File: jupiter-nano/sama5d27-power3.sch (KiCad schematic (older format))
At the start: 25 parts, among them U4 MIC5247-2.0YM5-TR

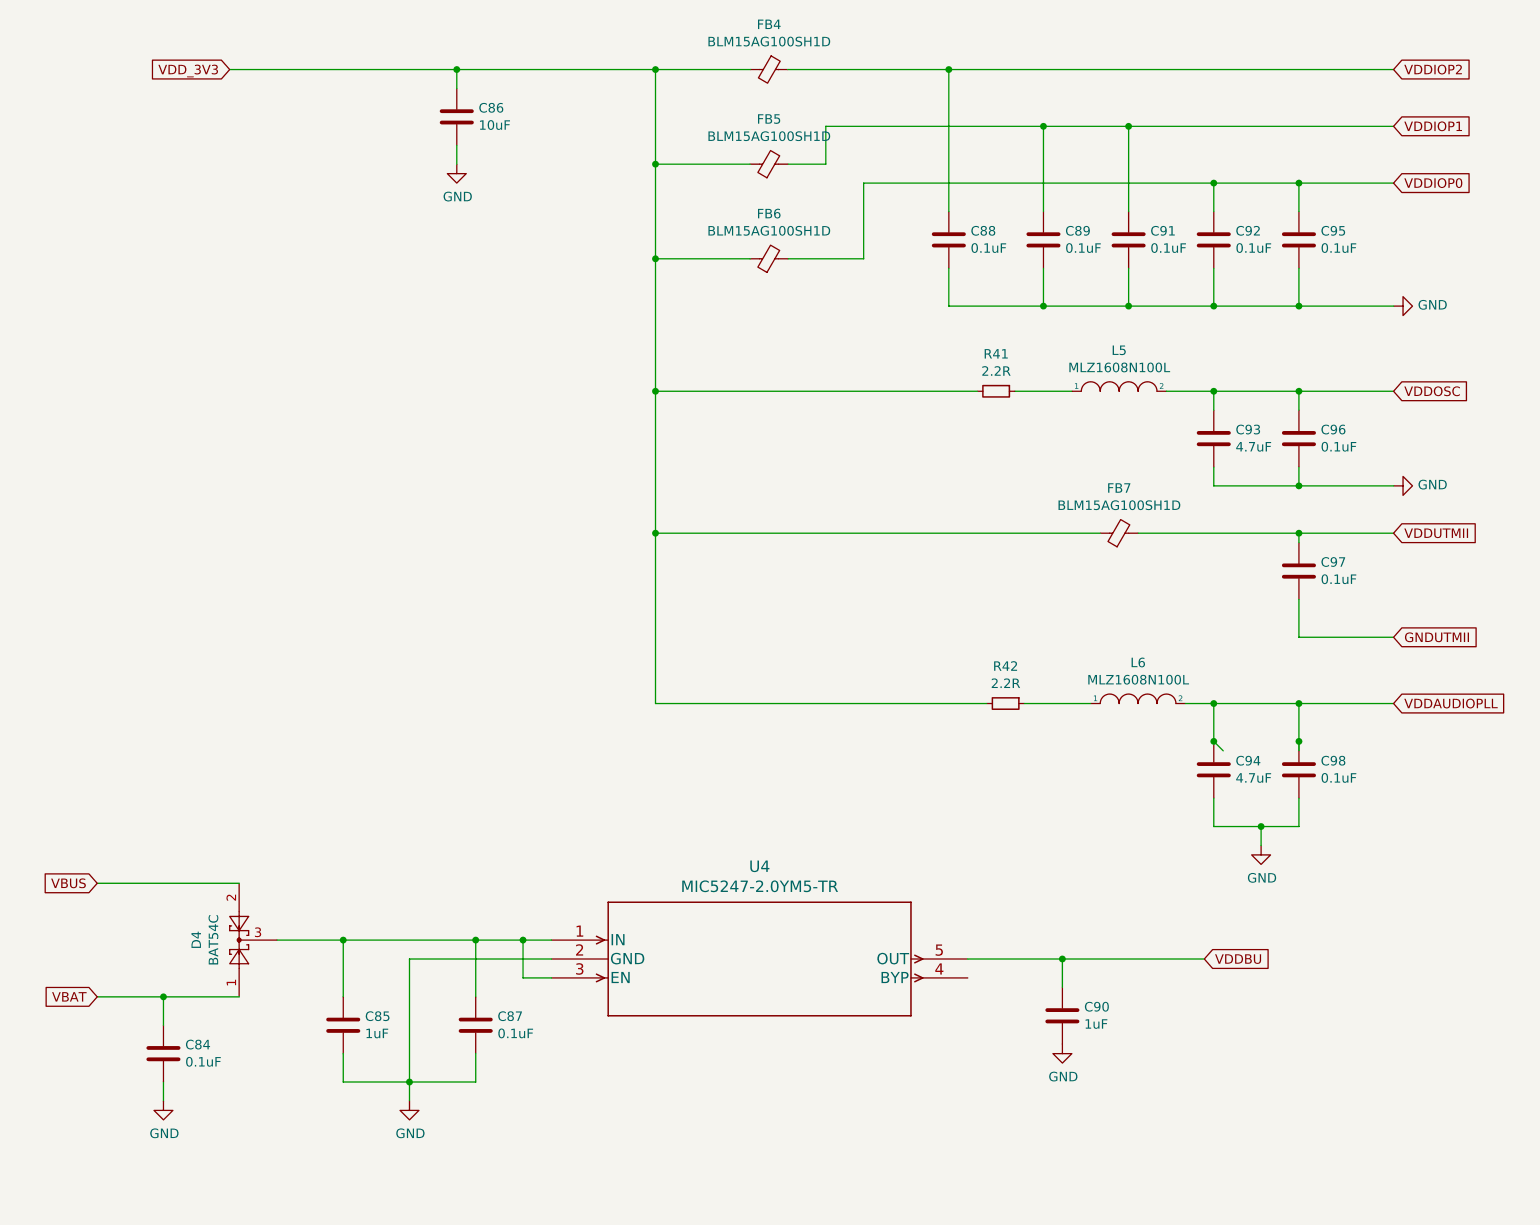
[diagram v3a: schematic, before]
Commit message: added at24csw080 I2C EEPROM UUID chip
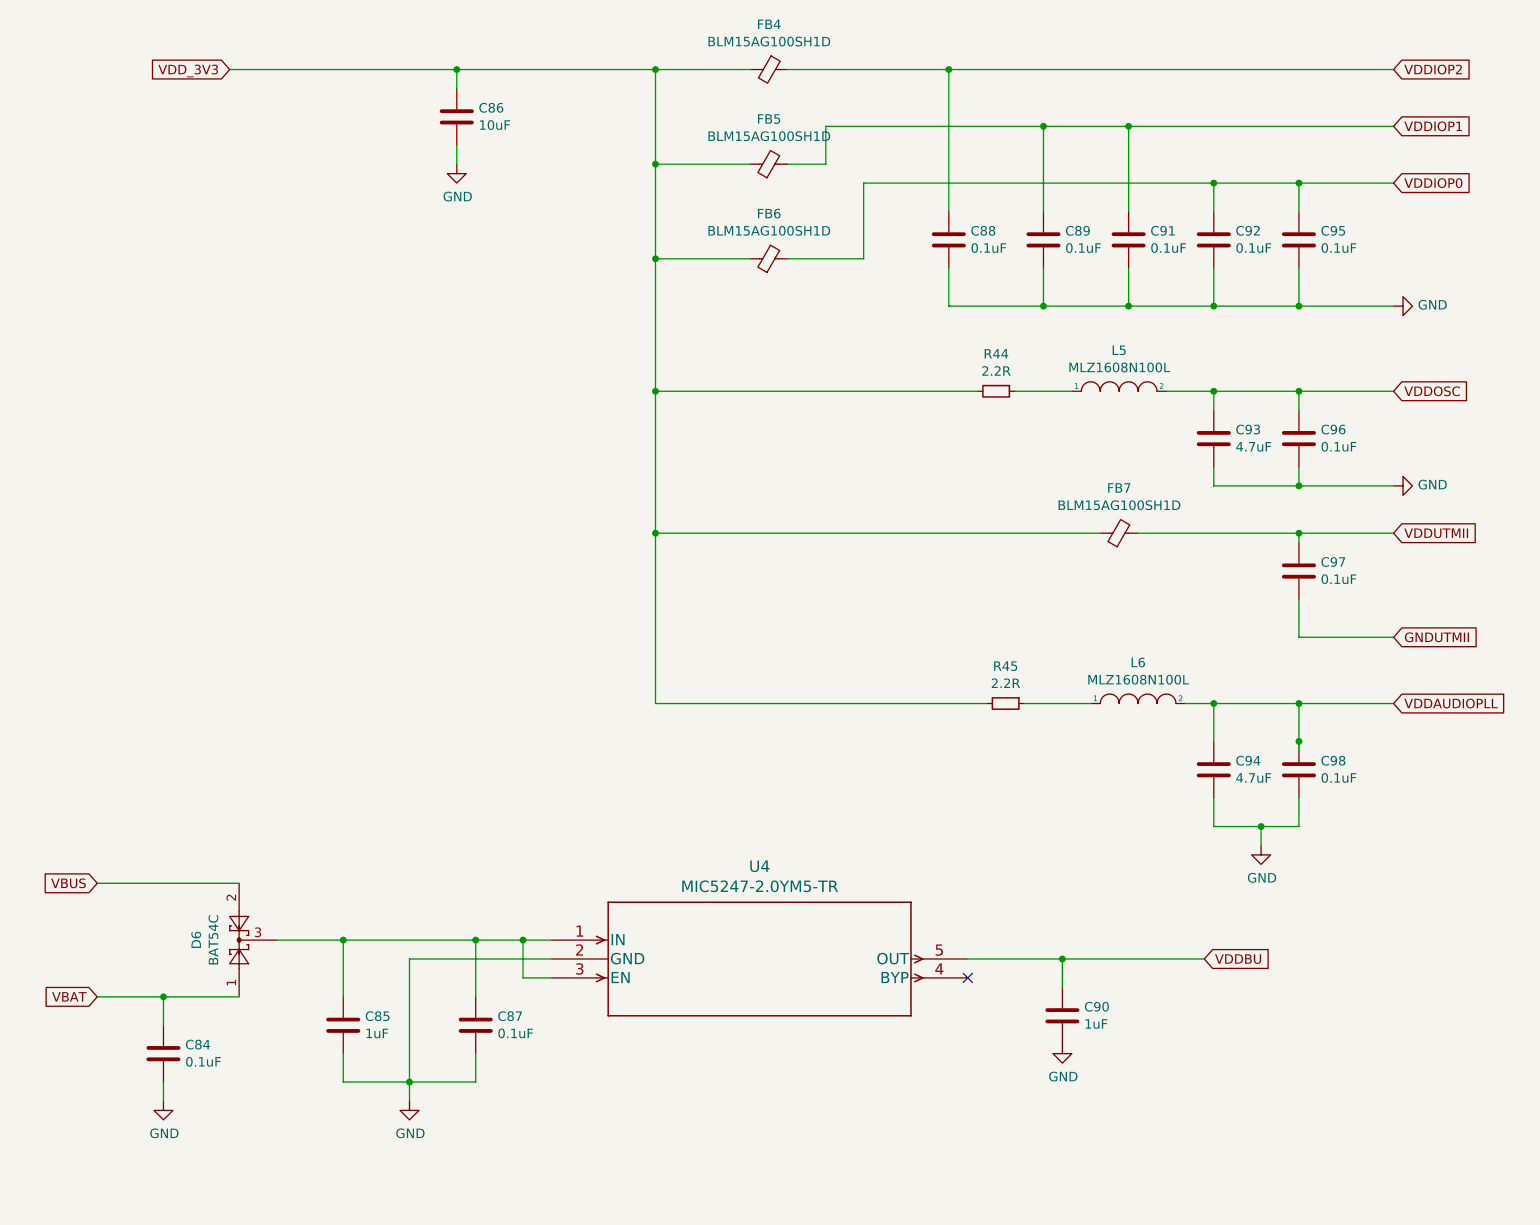
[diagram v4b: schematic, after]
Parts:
- renumbered D4 to D6, R41 to R44, R42 to R45
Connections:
- no-connect marks 0 -> 1
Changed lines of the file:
@@
 P 2200 5600
 AR Path="/5F395E67/5FD7EF78" Ref="D?"  Part="1"
-AR Path="/5FD740BF/5FD7EF78" Ref="D4"  Part="1"
-F 0 "D4" H 2200 5825 50  0000 C CNN
+AR Path="/5FD740BF/5FD7EF78" Ref="D6"  Part="1"
+F 0 "D6" H 2200 5825 50  0000 C CNN
 F 1 "BAT54C" H 2200 5734 50  0000 C CNN
 F 2 "Package_TO_SOT_SMD:SOT-23" H 2275 5725 50  0001 L CNN
@@
 	6550 5700 7300 5700
 $Comp
-L power:GND #PWR072
+L power:GND #PWR073
 U 1 1 5FD98CB8
 P 6550 6150
-F 0 "#PWR072" H 6550 5900 50  0001 C CNN
+F 0 "#PWR073" H 6550 5900 50  0001 C CNN
 F 1 "GND" H 6555 5977 50  0000 C CNN
 F 2 "" H 6550 6150 50  0001 C CNN
@@
 	3100 6350 3100 6450
 $Comp
-L power:GND #PWR070
+L power:GND #PWR071
 U 1 1 5FD9D491
 P 3100 6450
-F 0 "#PWR070" H 3100 6200 50  0001 C CNN
+F 0 "#PWR071" H 3100 6200 50  0001 C CNN
 F 1 "GND" H 3105 6277 50  0000 C CNN
 F 2 "" H 3100 6450 50  0001 C CNN
@@
 	1800 5900 1450 5900
 $Comp
-L power:GND #PWR069
+L power:GND #PWR070
 U 1 1 5FDA258D
 P 1800 6450
-F 0 "#PWR069" H 1800 6200 50  0001 C CNN
+F 0 "#PWR070" H 1800 6200 50  0001 C CNN
 F 1 "GND" H 1805 6277 50  0000 C CNN
 F 2 "" H 1800 6450 50  0001 C CNN
@@
 	5950 2250 6450 2250
 $Comp
-L power:GND #PWR074
+L power:GND #PWR075
 U 1 1 5FDA8E26
 P 8300 2250
-F 0 "#PWR074" H 8300 2000 50  0001 C CNN
+F 0 "#PWR075" H 8300 2000 50  0001 C CNN
 F 1 "GND" V 8305 2122 50  0000 R CNN
 F 2 "" H 8300 2250 50  0001 C CNN
@@
 Wire Wire Line
 	7800 4550 7800 4350
-Connection ~ 7350 4550
-Wire Wire Line
-	7350 4550 7400 4600
 Wire Wire Line
 	7600 5000 7600 5100
@@
 	7600 5000 7800 5000
 $Comp
-L power:GND #PWR073
+L power:GND #PWR074
 U 1 1 5FE0FC03
 P 7600 5100
-F 0 "#PWR073" H 7600 4850 50  0001 C CNN
+F 0 "#PWR074" H 7600 4850 50  0001 C CNN
 F 1 "GND" H 7605 4927 50  0000 C CNN
 F 2 "" H 7600 5100 50  0001 C CNN
@@
 	7800 3200 8300 3200
 $Comp
-L power:GND #PWR075
+L power:GND #PWR076
 U 1 1 5FE13F3A
 P 8300 3200
-F 0 "#PWR075" H 8300 2950 50  0001 C CNN
+F 0 "#PWR076" H 8300 2950 50  0001 C CNN
 F 1 "GND" V 8305 3072 50  0000 R CNN
 F 2 "" H 8300 3200 50  0001 C CNN
@@
 $EndComp
 $Comp
-L Device:R_Small R41
+L Device:R_Small R44
 U 1 1 5FE21466
 P 6200 2700
-F 0 "R41" V 6004 2700 50  0000 C CNN
+F 0 "R44" V 6004 2700 50  0000 C CNN
 F 1 "2.2R" V 6095 2700 50  0000 C CNN
 F 2 "" H 6200 2700 50  0001 C CNN
@@
 	3350 1400 3350 1500
 $Comp
-L power:GND #PWR071
+L power:GND #PWR072
 U 1 1 5FE4A1D6
 P 3350 1500
-F 0 "#PWR071" H 3350 1250 50  0001 C CNN
+F 0 "#PWR072" H 3350 1250 50  0001 C CNN
 F 1 "GND" H 3355 1327 50  0000 C CNN
 F 2 "" H 3350 1500 50  0001 C CNN
@@
 $EndComp
 $Comp
-L Device:R_Small R42
+L Device:R_Small R45
 U 1 1 5FE4B82E
 P 6250 4350
-F 0 "R42" V 6054 4350 50  0000 C CNN
+F 0 "R45" V 6054 4350 50  0000 C CNN
 F 1 "2.2R" V 6145 4350 50  0000 C CNN
 F 2 "" H 6250 4350 50  0001 C CNN
@@
 	6950 3450 7800 3450
 Connection ~ 7800 3450
+NoConn ~ 6050 5800
 $EndSCHEMATC
